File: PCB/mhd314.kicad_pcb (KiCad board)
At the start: 4 copper layers, 65 x 56 mm, 197 parts, among them J1 Raspberry_Pi_2_3, J2 AudioJack_Pentaconn, J4 AudioJack3_SwitchTR, Q1 AO3401A, SW1 SW_Push, U1 ES9038Q2M, U10 AT24CS64-SSHM, U11 OPA1622, U12 OPA1622, U13 OPA1622, U14 OPA1622, U2 OPA1612AxD, U3 OPA1612AxD, U4 OPA1622, U5 LM317_SOT-223, U6 LM317_SOT-223, U7 TPS65131RGE, U8 LM317_SOT-223, U9 LM337_SOT223, X1 ASCO

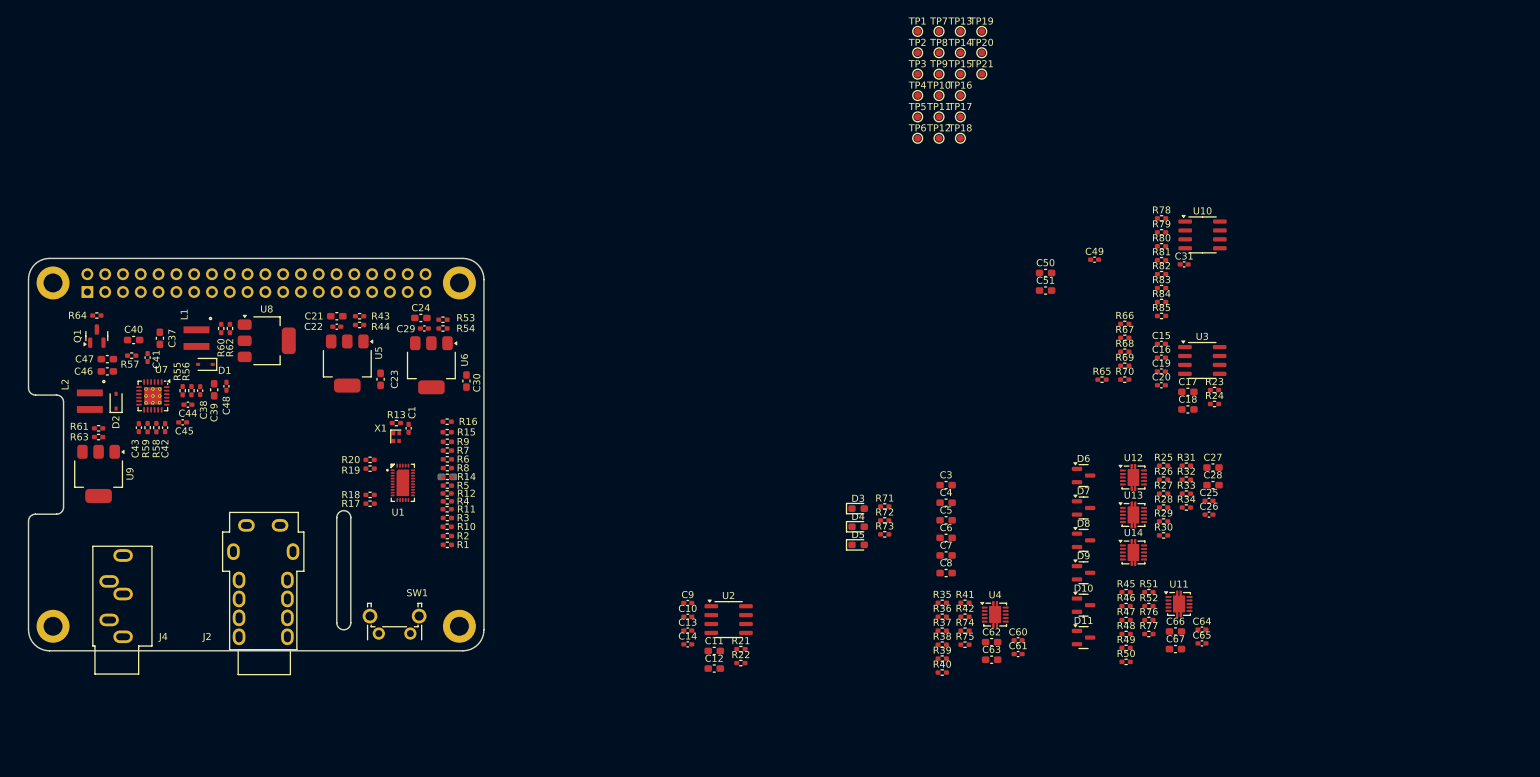
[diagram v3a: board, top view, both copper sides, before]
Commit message: Finished basic placement
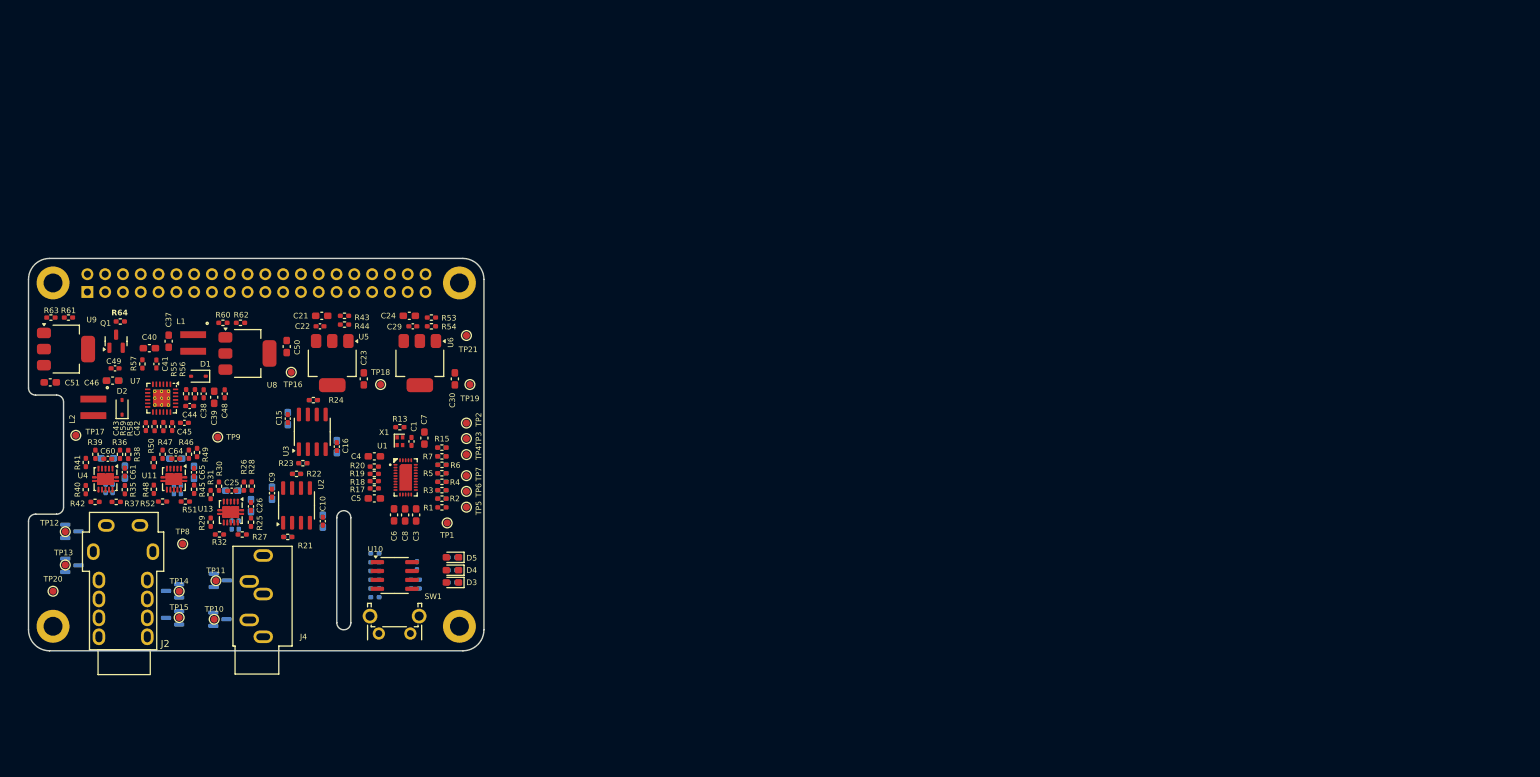
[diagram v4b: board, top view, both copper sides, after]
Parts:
- removed C2: 1uF, Capacitor_SMD:C_0603_1608Metric_Pad1.08x0.95mm_HandSolder
- removed R65, R66, R67, R68, R69, R70: 0R, Resistor_SMD:R_0402_1005Metric_Pad0.72x0.64mm_HandSolder
- removed U12, U14: OPA1622, Package_SON:Texas_S-PVSON-N10
- C11, C12, C13, C14, C17, C18, C19, C20, C27, C28, C31, C47, C62, C63, C66, C67, D10, D11, D6, D7, D8, D9, R10, R11, R12, R16, R33, R34, R71, R72, R73, R74, R75, R76, R77, R78, R79, R8, R80, R81, R82, R83, R84, R85, R9: moved to B.Cu
- R14: value 100k -> 10k; moved to B.Cu
- moved TP20 153.2 mm to (70.0, 103.8)
- moved TP13 148.7 mm to (71.8, 100.0)
- moved C64 148.5 mm to (87.5, 84.8), turned to 180 degrees
- moved C65 145.9 mm to (90.1, 86.8), turned to -90 degrees
- moved C66 144.8 mm to (87.5, 84.8), turned to 180 degrees
- moved U11 144.6 mm to (87.2, 87.8), turned to -90 degrees
- moved D8 144.4 mm to (72.7, 95.2)
- moved D9 144.4 mm to (72.7, 100.0)
- moved C51 142.7 mm to (69.6, 73.9)
- moved C67 142.3 mm to (90.1, 86.8), turned to -90 degrees
- moved R50 141.7 mm to (84.4, 85.4), turned to -90 degrees
- moved R52 141.6 mm to (85.6, 91.0)
- moved R77 140.7 mm to (87.2, 89.2), turned to 90 degrees
- moved C49 140.7 mm to (78.8, 71.9), turned to 180 degrees
- moved R48 140.3 mm to (84.4, 89.2), turned to -90 degrees
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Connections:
- C23 pad 1: +3.3V1 -> +3.3VA
- C30 pad 1: +3.3V2 -> +3.3V
- R25 pad 2: Net-(U12A--) -> Net-(U13A--)
- R26 pad 2: Net-(U12A-+) -> Net-(U13A-+)
- R27 pad 1: Net-(U12A--) -> Net-(U13A--)
- R28 pad 2: Net-(U12A-+) -> Net-(U13A-+)
- R29 pad 2: Net-(U13A--) -> Net-(U13B--)
- R30 pad 2: Net-(U13A-+) -> Net-(U13B-+)
- R31 pad 2: Net-(U13A-+) -> Net-(U13B-+)
- R32 pad 1: Net-(U13A--) -> Net-(U13B--)
- R33 pad 2: Net-(U12A-EN) -> Net-(U13A-EN)
- R34 pad 1: Net-(U12A-EN) -> Net-(U13A-EN)
- R44 pad 1: +3.3V1 -> +3.3VA
- R54 pad 1: +3.3V2 -> +3.3V
- TP1 pad 1: /BRD_ONOFF -> /DAC_SPDIF
- U11 pad 11: (no net) -> -5VA
- U11 pad 2: (no net) -> +5VA
- U11 pad 3: (no net) -> GND
- U11 pad 4: (no net) -> -5VA
- U13 pad 5: (no net) -> Net-(U13B-+)
- U13 pad 6: (no net) -> Net-(U13B--)
- U13 pad 7: (no net) -> /OUT_SE_R
- U13 pad 8: unconnected-(U13A-EN-Pad8) -> Net-(U13A-EN)
- U13 pad 9: /OUT_SE_R -> /OUT_SE_L
- U4 pad 11: (no net) -> -5VA
- U4 pad 2: (no net) -> +5VA
- U4 pad 3: (no net) -> GND
- U4 pad 4: (no net) -> -5VA
- U5 pad 2: +3.3V1 -> +3.3VA
- U6 pad 2: +3.3V2 -> +3.3V

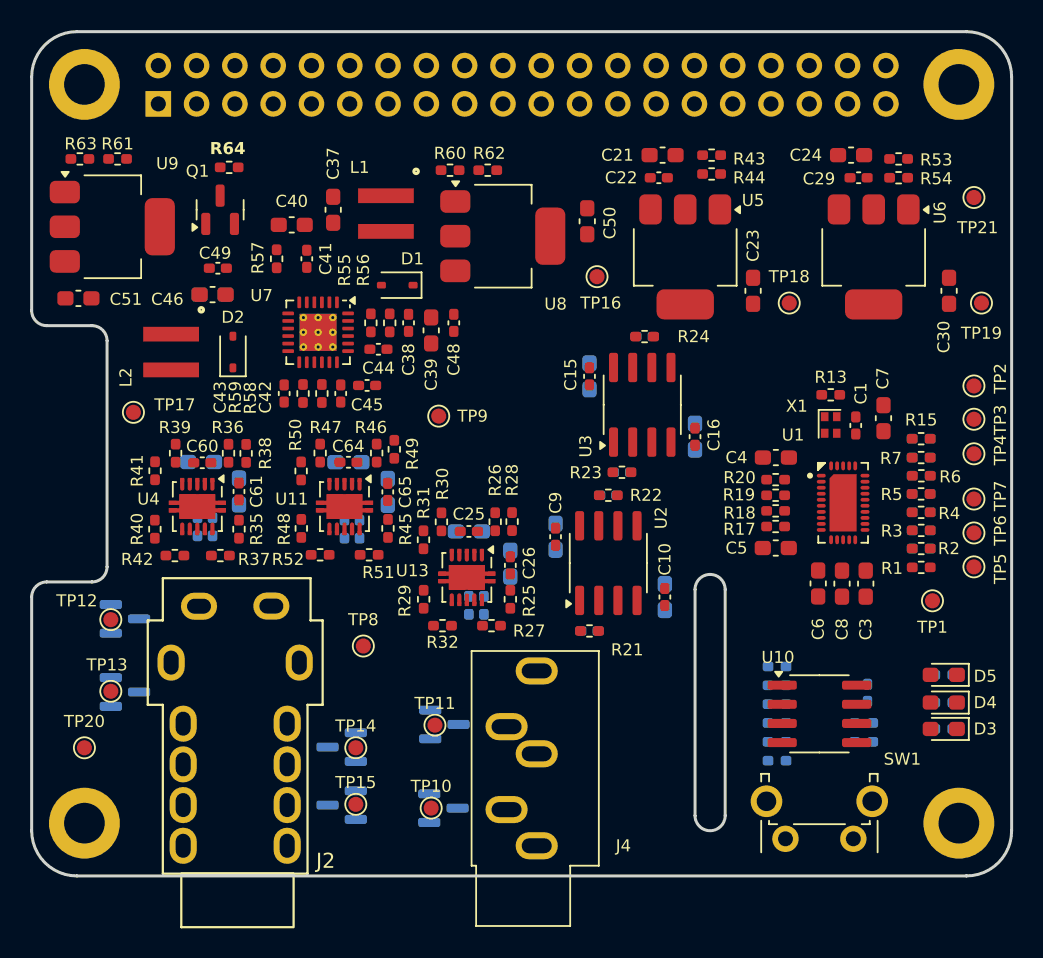
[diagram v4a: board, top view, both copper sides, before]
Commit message: Routed power section
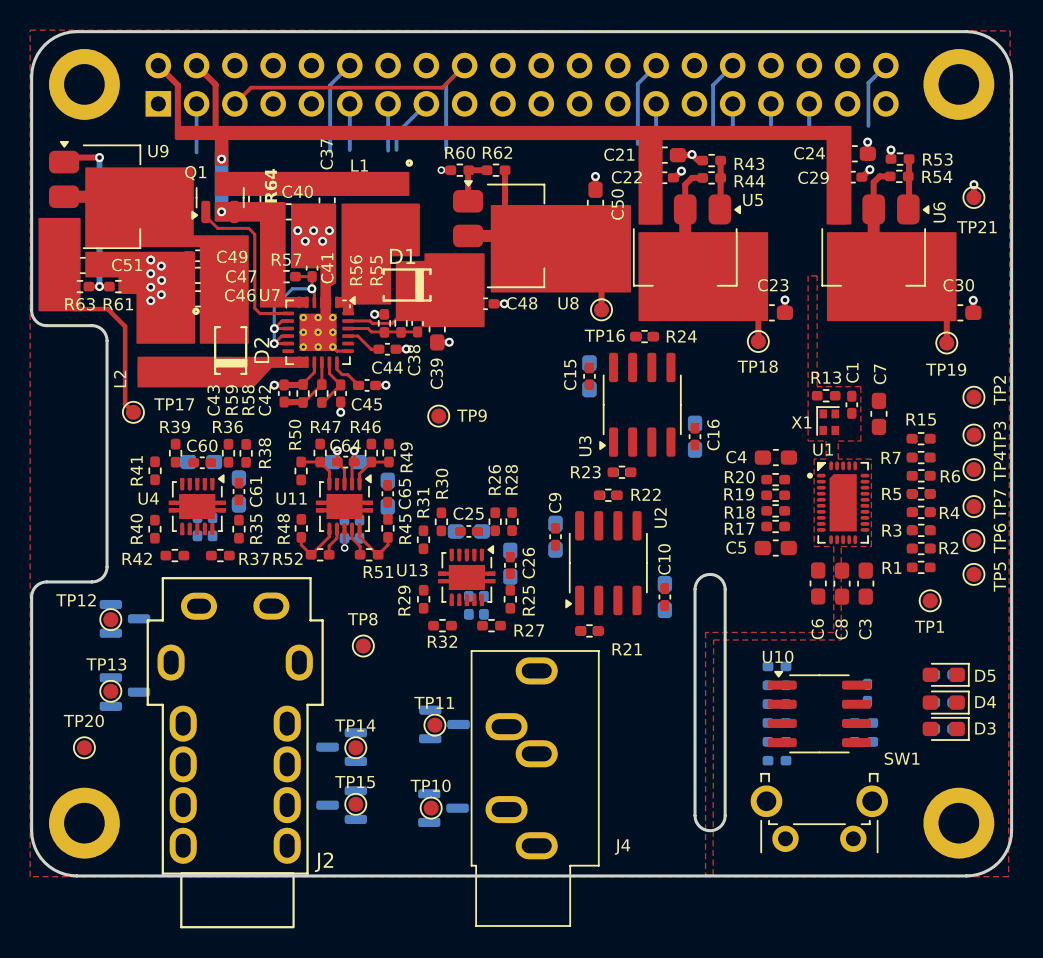
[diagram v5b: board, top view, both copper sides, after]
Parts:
- C47: moved to F.Cu
- D1, D2: value 1N5819WS -> MBR130T1G; footprint Diode_SMD:D_SOD-323 -> _mahaudio KiCad Library:SOD-123_425-04_ONS
- moved R61 8.47 mm to (72.2, 73.2)
- moved R63 8.47 mm to (69.7, 73.2)
- moved TP19 3.51 mm to (127.2, 76.9)
- moved TP18 3.27 mm to (114.7, 76.8)
- moved R64 2.70 mm to (81.3, 67.3), turned to 90 degrees
- moved C48 2.45 mm to (96.6, 74.3), turned to 0 degrees
- moved TP16 2.22 mm to (104.3, 74.7)
- moved C51 2.20 mm to (69.9, 71.8)
- moved R55 2.00 mm to (91.0, 75.6)
- moved U9 1.99 mm to (71.8, 67.2)
- moved C23 1.92 mm to (115.6, 74.9), turned to 0 degrees
- moved C30 1.64 mm to (128.1, 74.9), turned to 0 degrees
- moved C47 1.61 mm to (77.5, 72.4)
- moved C49 1.57 mm to (77.5, 71.1)
- moved C1 1.40 mm to (120.9, 81.0), turned to 90 degrees
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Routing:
- net /BRD_ONOFF: track 0.00 -> 22.4 mm
- net +5VA: track 0.00 -> 18.5 mm, vias 0 -> 1
- net GND: track 0.00 -> 17.1 mm, vias 0 -> 29
- net Net-(U7-ENN): track 0.00 -> 12.6 mm, vias 0 -> 3
- net Net-(U9-ADJ): track 0.00 -> 12.4 mm, vias 0 -> 2
- net +3.3VA: track 0.00 -> 11.5 mm
- net +3.3V: track 0.00 -> 11.4 mm
- net Net-(Q1-G): track 0.00 -> 11.3 mm
- net +5VIN: track 0.00 -> 10.2 mm, vias 0 -> 2
- net -8VA: track 0.00 -> 10.0 mm, vias 0 -> 1
- net -5VA: track 0.00 -> 9.80 mm
- net /DAC_PCM_CLK: track 0.00 -> 6.24 mm
- net /BRD_ID_SC: track 0.00 -> 5.71 mm
- net /BRD_LED0: track 0.00 -> 5.24 mm
- net Net-(U7-FBP): track 0.00 -> 4.71 mm
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- added copper zone on F.Cu, net GND
- added copper zone on In1.Cu, net GND

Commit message: Routed DAC section
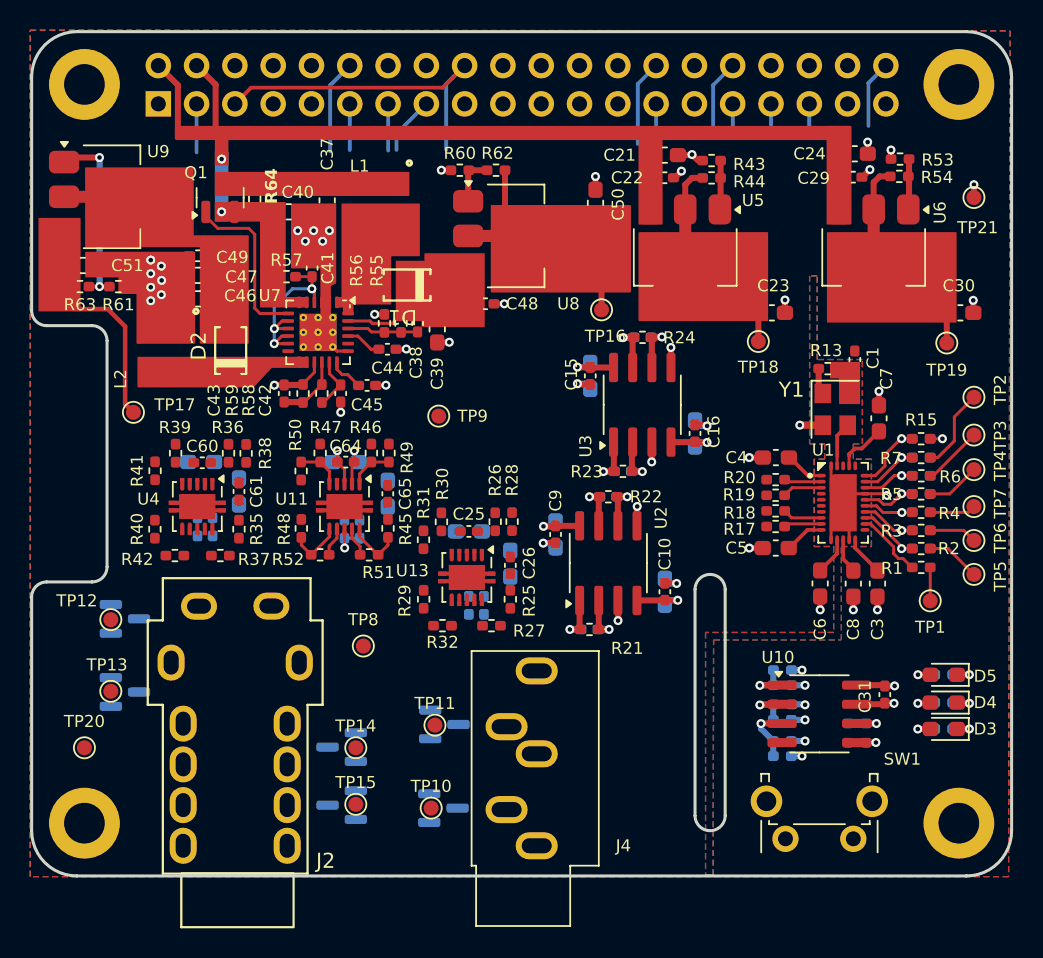
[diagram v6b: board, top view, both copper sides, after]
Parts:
- removed X1: ASCO, Oscillator:Oscillator_SMD_Abracon_ASCO-4Pin_1.6x1.2mm
- added Y1: ASE-50MHz, Oscillator:Oscillator_SMD_Abracon_ASE-4Pin_3.2x2.5mm, F.Cu at (119.8, 81.3)
- C31: moved to F.Cu
- moved R73 3.60 mm to (127.0, 98.9)
- moved R71 3.59 mm to (127.0, 102.5)
- moved C1 3.01 mm to (121.1, 78.0)
- moved R13 1.80 mm to (119.3, 78.6)
- moved R79 1.30 mm to (116.3, 99.6)
- moved C31 1.15 mm to (123.1, 100.2)
- moved R78 1.07 mm to (116.3, 98.6)
- moved C3 0.78 mm to (122.6, 92.9)
- moved C8 0.75 mm to (121.0, 92.9)
- moved R83 0.46 mm to (116.3, 104.3)
- moved R85 0.46 mm to (121.2, 103.4)
- moved R84 0.44 mm to (121.2, 102.1)
- moved R81 0.41 mm to (116.3, 101.9)
- moved R80 0.38 mm to (116.3, 100.9)
- moved R82 0.35 mm to (116.3, 103.3)
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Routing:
- net GND: track 17.1 -> 55.6 mm, vias 29 -> 52
- net +3.3VA: track 11.5 -> 22.7 mm
- net +3.3V: track 11.4 -> 19.6 mm, vias 0 -> 5
- net -5VA: track 9.80 -> 16.8 mm, vias 0 -> 2
- net +5VA: track 18.5 -> 25.3 mm, vias 1 -> 3
- net /DAC_SDA: track 3.22 -> 8.72 mm
- net Net-(U1-ADDR): track 0.00 -> 5.28 mm, vias 0 -> 1
- net Net-(U1-DATA2): track 0.00 -> 4.75 mm, vias 0 -> 1
- net Net-(U1-GPIO1): track 0.00 -> 4.59 mm
- net Net-(U1-SDA): track 0.00 -> 4.50 mm, vias 0 -> 1
- net Net-(U1-DATA1): track 0.00 -> 4.34 mm, vias 0 -> 1
- net Net-(U1-RESETB): track 0.00 -> 4.24 mm, vias 0 -> 1
- net Net-(U1-SCL): track 0.00 -> 4.16 mm, vias 0 -> 1
- net Net-(U1-DATA_CLK): track 0.00 -> 4.03 mm, vias 0 -> 1
- net /BRD_ONOFF: track 22.4 -> 26.4 mm
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- added copper zone on B.Cu, net GND

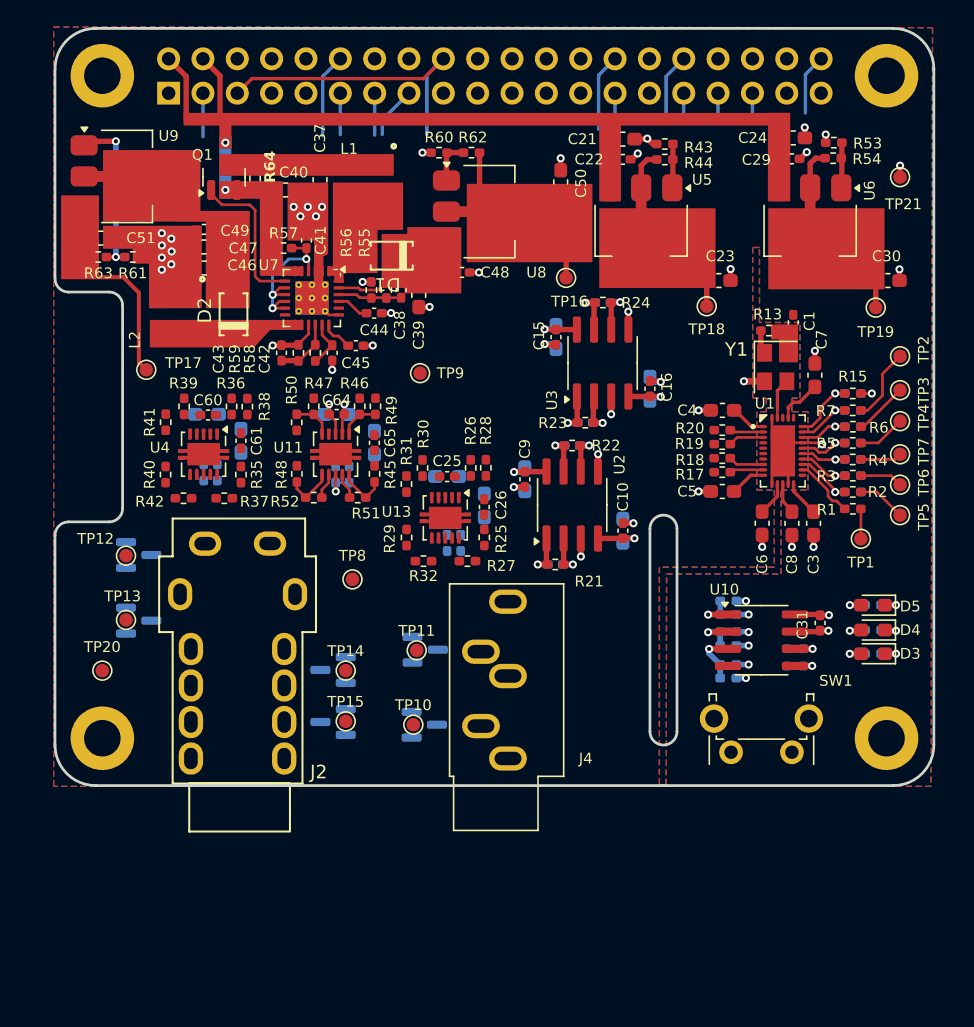
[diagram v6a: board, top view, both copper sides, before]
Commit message: Routed single ended path and moved some components to top side
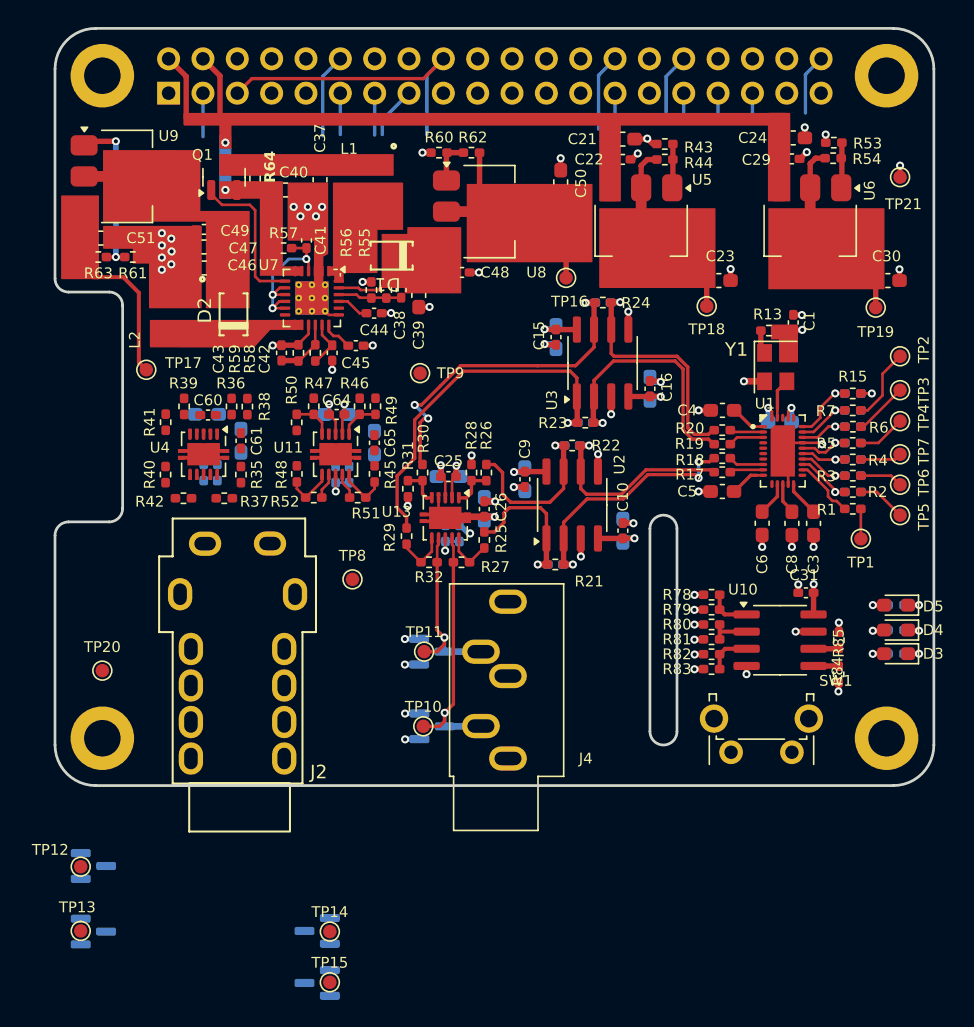
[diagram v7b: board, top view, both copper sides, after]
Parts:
- C7: moved to B.Cu
- R78, R79, R80, R81, R82, R83, R84, R85: moved to F.Cu
- moved D8 23.2 mm to (69.3, 118.2)
- moved D9 23.2 mm to (69.3, 123.0)
- moved TP12 23.2 mm to (68.4, 118.2)
- moved TP13 23.2 mm to (68.4, 123.0)
- moved D10 19.3 mm to (85.9, 123.0)
- moved D11 19.3 mm to (85.9, 126.8)
- moved TP14 19.3 mm to (86.8, 123.0)
- moved TP15 19.3 mm to (86.8, 126.8)
- moved C7 4.33 mm to (120.1, 85.4), turned to 180 degrees
- moved R84 3.29 mm to (124.5, 101.5), turned to 90 degrees
- moved R85 3.29 mm to (124.5, 104.0), turned to -90 degrees
- moved C31 2.46 mm to (122.0, 98.0), turned to 180 degrees
- moved D3 1.70 mm to (128.7, 102.5)
- moved D4 1.70 mm to (128.7, 100.8)
- moved D5 1.70 mm to (128.7, 98.9)
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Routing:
- net /AMP/BalDiffAmp_R/BALDIFFAMP_IN_P: track 3.39 -> 27.3 mm
- net /AMP/BalDiffAmp_R/BALDIFFAMP_IN_N: track 3.43 -> 25.1 mm, vias 1 -> 3
- net /OUT_SE_L: track 0.00 -> 19.3 mm, vias 0 -> 1
- net /DAC_OUT_R_P: track 3.38 -> 19.2 mm
- net /DAC_OUT_L_P: track 3.37 -> 18.6 mm, vias 1 -> 3
- net /DAC_OUT_R_N: track 3.43 -> 18.1 mm
- net /OUT_SE_R: track 0.00 -> 13.6 mm, vias 0 -> 1
- net /DAC_OUT_L_N: track 3.28 -> 15.4 mm
- net /AMP/BalDiffAmp_L/BALDIFFAMP_IN_N: track 3.28 -> 12.8 mm
- net /AMP/BalDiffAmp_L/BALDIFFAMP_IN_P: track 3.38 -> 11.1 mm
- net -5VA: track 16.8 -> 24.5 mm, vias 2 -> 5
- net +5VA: track 25.3 -> 30.8 mm, vias 3 -> 6
- net GND: track 55.6 -> 61.0 mm, vias 52 -> 60
- net Net-(U13B--): track 0.00 -> 3.92 mm
- net Net-(U13A--): track 0.00 -> 3.67 mm
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- removed copper zone on B.Cu, net GND
- removed copper zone on F.Cu, net GND
